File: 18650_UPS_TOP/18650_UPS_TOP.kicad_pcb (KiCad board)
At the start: 2 copper layers, 90 x 25.5 mm, 16 parts, among them U1 OLED_30_Pin, U2 APX803

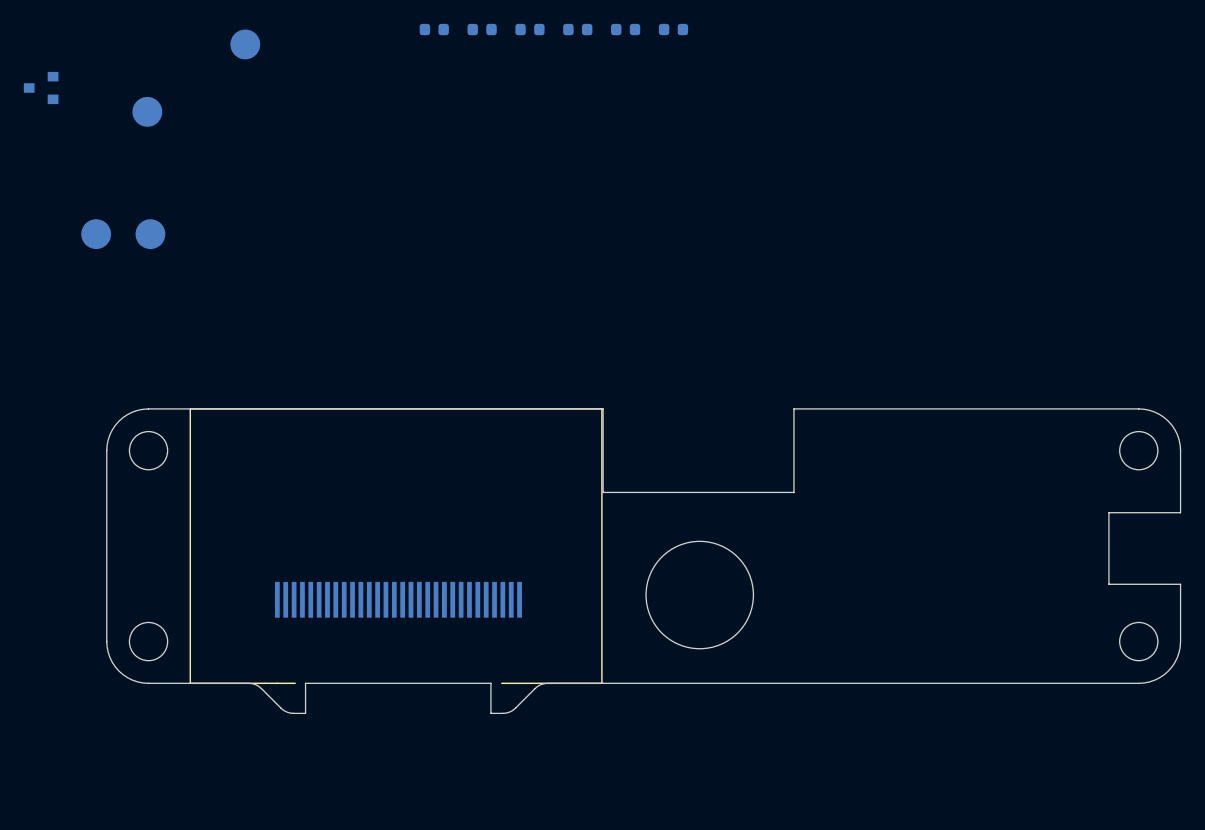
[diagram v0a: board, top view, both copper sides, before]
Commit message: changed buttons
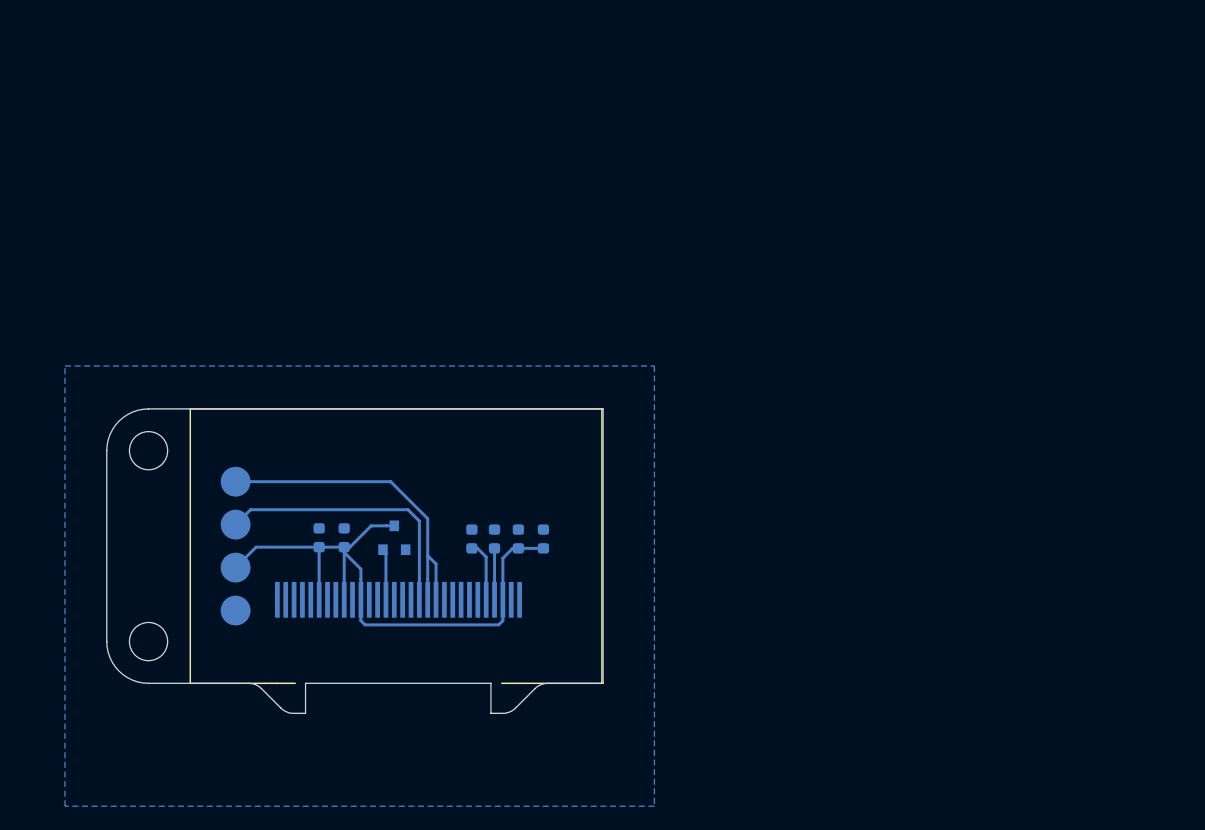
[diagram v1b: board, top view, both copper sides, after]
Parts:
- removed H2, H4: MountingHole, MountingHole:MountingHole_3.2mm_M3
- removed e: TestPoint, TestPoint:TestPoint_Pad_D2.5mm
- added TP2: TestPoint, TestPoint:TestPoint_Pad_D2.5mm, B.Cu at (77.4, 83.2)
- moved C1 50.8 mm to (86.5, 84.3), turned to 90 degrees
- moved C2 49.7 mm to (84.4, 84.3), turned to 90 degrees
- moved U2 47.9 mm to (90.7, 84.3), turned to 90 degrees
- moved C3 43.3 mm to (99.1, 84.4), turned to 90 degrees
- moved C5 43.0 mm to (103.2, 84.4), turned to 90 degrees
- moved R1 42.8 mm to (97.2, 84.4), turned to 90 degrees
- moved C4 42.7 mm to (101.1, 84.4), turned to 90 degrees
- moved TP4 42.4 mm to (77.4, 90.4)
- moved TP3 30.3 mm to (77.4, 86.8)
- moved TP1 21.9 mm to (77.4, 79.6)
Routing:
- net +3V3: track 0.00 -> 51.5 mm
- net I2C1_SDA: track 0.00 -> 28.2 mm
- net I2C1_SCL: track 0.00 -> 22.9 mm
- net Net-(R1-Pad1): track 0.00 -> 5.09 mm
- net Net-(C3-Pad1): track 0.00 -> 4.31 mm
- net Net-(U1-Pad14): track 0.00 -> 4.30 mm
- added copper zone on B.Cu, net GND
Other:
- board size 90 x 25.5 mm -> 41.6 x 25.5 mm
- board text added: "3V3"
- board text added: "GND"
- board text added: "SCL"
- board text added: "SDA"
